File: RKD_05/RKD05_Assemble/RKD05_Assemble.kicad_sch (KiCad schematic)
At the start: 150 parts, among them J3 Conn_01x24, M1 Mark, M2 Mark, M3 Mark, M4 Mark, M5 Mark, M6 Mark, M7 Mark, SW1 SW_Push, SW10 SW_Push, SW11 SW_Push, SW12 SW_Push, SW13 SW_Push, SW14 SW_Push, SW15 SW_Push, SW16 SW_Push, SW17 SW_Push, SW18 SW_Push, SW19 SW_Push, SW2 SW_Push, SW20 SW_Push, SW21 SW_Push, SW22 SW_Push, SW23 SW_Push, SW24 SW_Push, SW25 SW_Push, SW26 SW_Push, SW27 SW_Push, SW28 SW_Push, SW29 SW_Push, SW3 SW_Push, SW30 SW_Push, SW4 SW_Push, SW40 RotaryEncoder_Switch, SW5 SW_Push, SW51 SW_Push, SW52 SW_Push, SW53 SW_Push, SW54 SW_Push, SW55 SW_Push, SW56 SW_Push, SW57 SW_Push, SW58 SW_Push, SW59 SW_Push, SW6 SW_Push, SW60 SW_Push, SW61 SW_Push, SW62 SW_Push, SW63 SW_Push, SW64 SW_Push, SW65 SW_Push, SW66 SW_Push, SW67 SW_Push, SW68 SW_Push, SW69 SW_Push, SW7 SW_Push, SW70 SW_Push, SW71 SW_Push, SW72 SW_Push, SW73 SW_Push, SW74 SW_Push, SW75 SW_Push, SW76 SW_Push, SW77 SW_Push, SW78 SW_Push, SW79 SW_Push, SW8 SW_Push, SW80 SW_Push, SW81 SW_Push, SW82 SW_Push, SW83 SW_Push, SW84 SW_Push, SW85 SW_Push, SW86 SW_Push, SW87 SW_Push, SW88 SW_Push, SW89 SW_Push, SW9 SW_Push, SW90 SW_Push

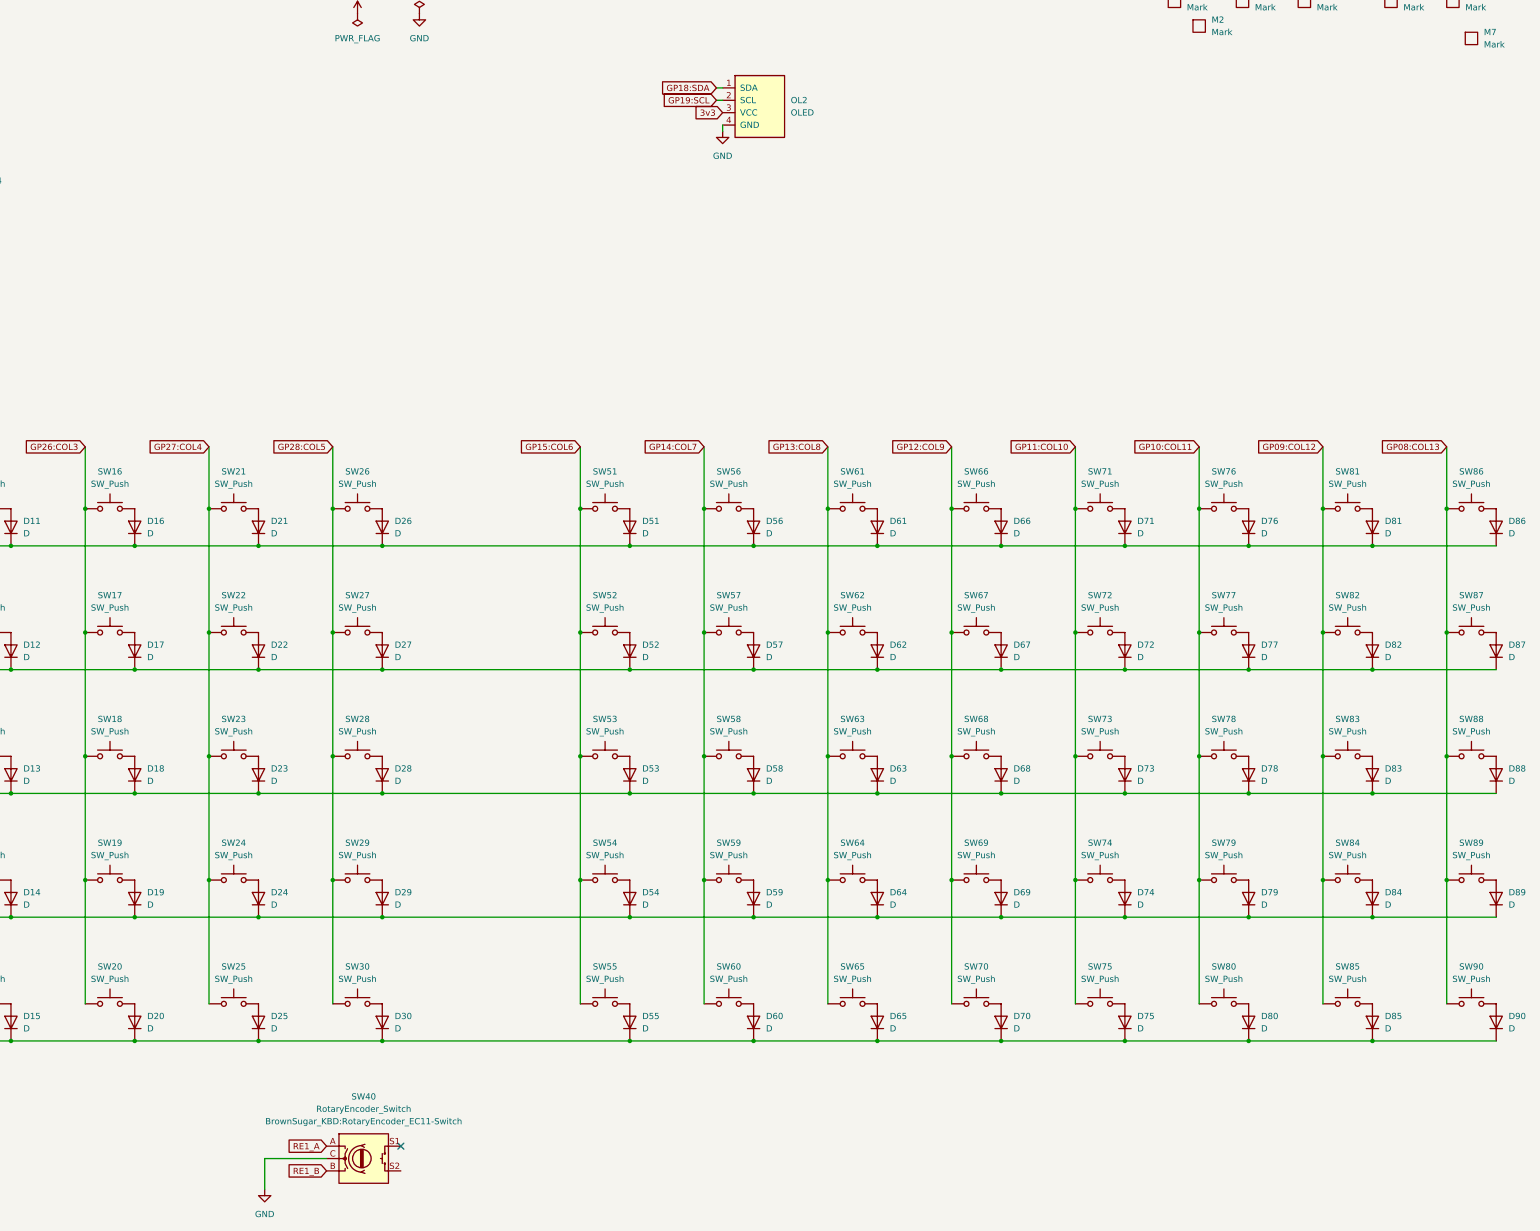
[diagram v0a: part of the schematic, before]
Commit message: RKD05　RE用PIN追加
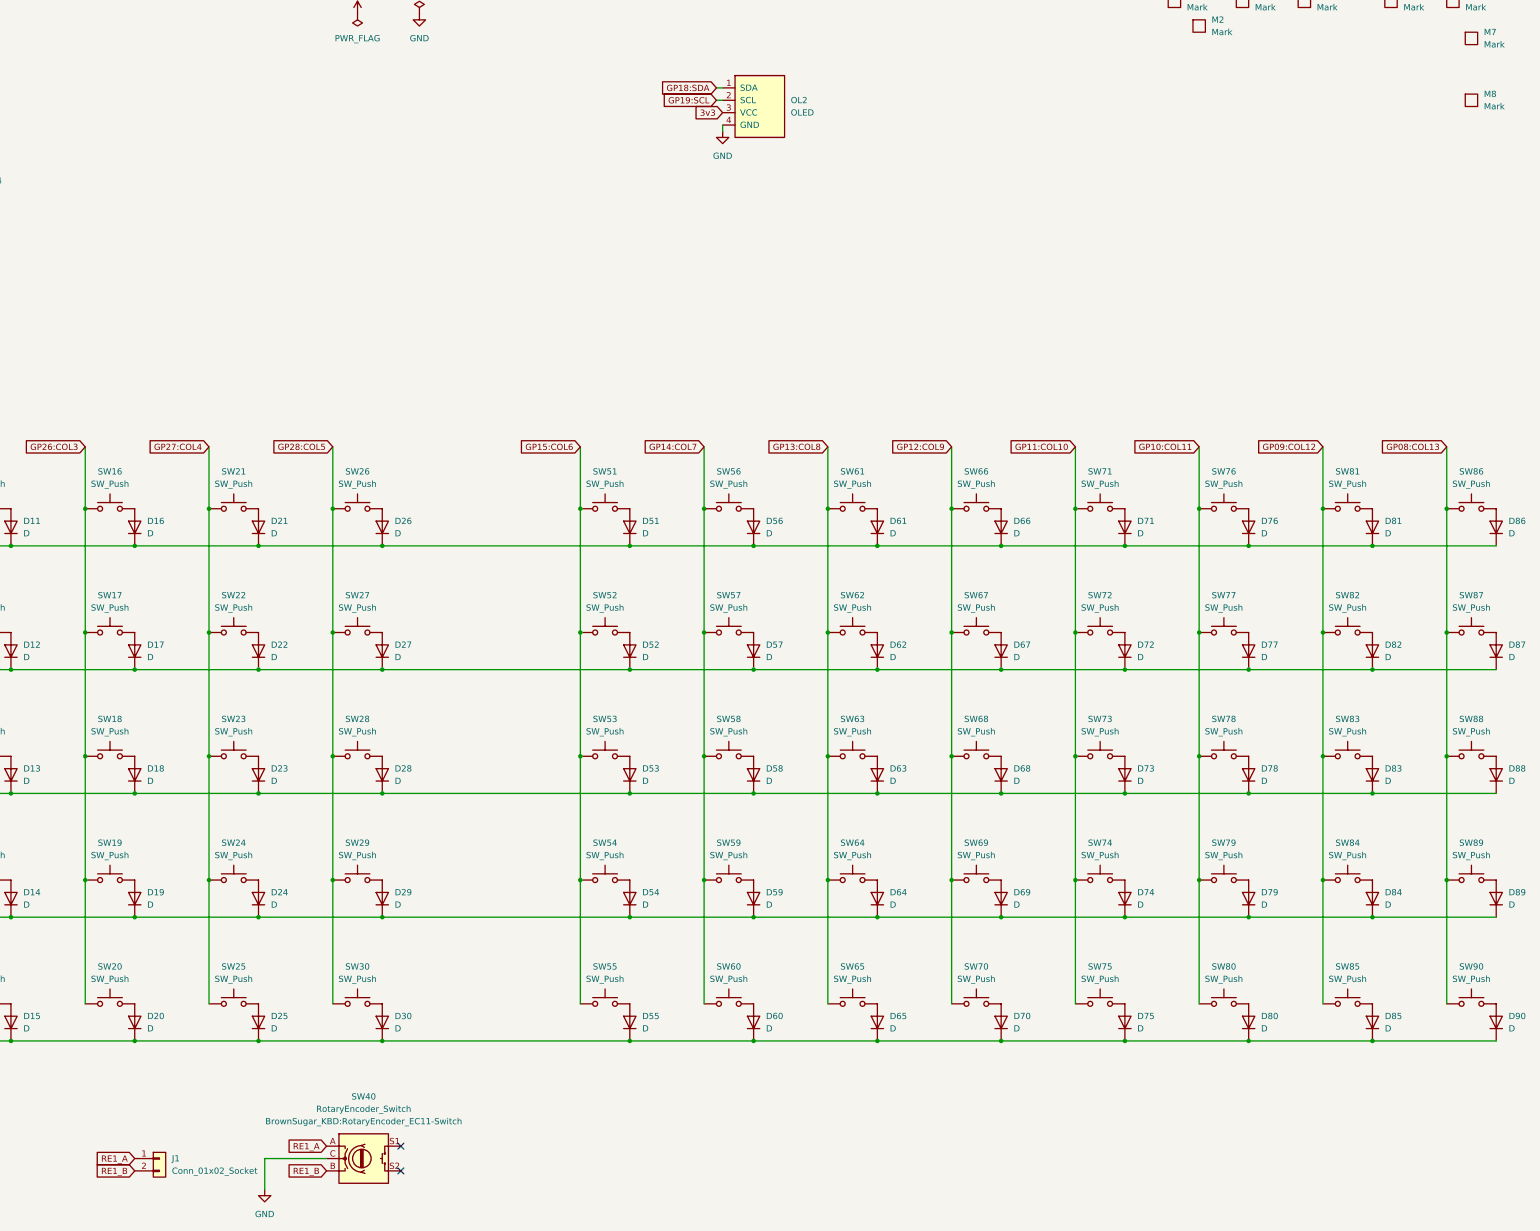
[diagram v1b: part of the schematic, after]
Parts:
- added J1: Conn_01x02_Socket, Connector_PinHeader_2.54mm:PinHeader_1x02_P2.54mm_Horizontal, symbol Connector_Generic:Conn_01x02
- added M8: Mark, Rikkodo_FootPrint:rkd_LOGO_2x, symbol BrownSugar_KBD:Mark
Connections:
- net RE1_A: now also J1.1 (Pin_1)
- net RE1_B: now also J1.2 (Pin_2)
- no-connect marks 1 -> 2
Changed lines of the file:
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@@
 	)
 	(no_connect
+		(at 173.99 262.89)
+	)
+	(no_connect
 		(at 173.99 257.81)
 	)
@@
 		)
 	)
+	(global_label "RE1_B"
+		(shape input)
+		(at 119.38 262.89 180)
+		(fields_autoplaced yes)
+		(effects
+			(font
+				(size 1.27 1.27)
+			)
+			(justify right)
+		)
+		(property "Intersheetrefs" "${INTERSHEET_REFS}"
+			(at 110.5287 262.89 0)
+			(effects
+				(font
+					(size 1.27 1.27)
+				)
+				(justify right)
+				(hide yes)
+			)
+		)
+	)
 	(global_label "GP15:COL6"
 		(shape input)
@@
 		)
 	)
+	(global_label "RE1_A"
+		(shape input)
+		(at 119.38 260.35 180)
+		(fields_autoplaced yes)
+		(effects
+			(font
+				(size 1.27 1.27)
+			)
+			(justify right)
+		)
+		(property "Intersheetrefs" "${INTERSHEET_REFS}"
+			(at 110.7101 260.35 0)
+			(effects
+				(font
+					(size 1.27 1.27)
+				)
+				(justify right)
+				(hide yes)
+			)
+		)
+	)
 	(global_label "GP20:ROW2"
 		(shape input)
@@
 	)
 	(symbol
+		(lib_id "BrownSugar_KBD:Mark")
+		(at 393.7 43.18 0)
+		(unit 1)
+		(exclude_from_sim no)
+		(in_bom yes)
+		(on_board yes)
+		(dnp no)
+		(fields_autoplaced yes)
+		(property "Reference" "M8"
+			(at 396.24 41.9099 0)
+			(effects
+				(font
+					(size 1.27 1.27)
+				)
+				(justify left)
+			)
+		)
+		(property "Value" "Mark"
+			(at 396.24 44.4499 0)
+			(effects
+				(font
+					(size 1.27 1.27)
+				)
+				(justify left)
+			)
+		)
+		(property "Footprint" "Rikkodo_FootPrint:rkd_LOGO_2x"
+			(at 393.7 43.18 0)
+			(effects
+				(font
+					(size 1.27 1.27)
+				)
+				(hide yes)
+			)
+		)
+		(property "Datasheet" ""
+			(at 393.7 43.18 0)
+			(effects
+				(font
+					(size 1.27 1.27)
+				)
+				(hide yes)
+			)
+		)
+		(property "Description" ""
+			(at 393.7 43.18 0)
+			(effects
+				(font
+					(size 1.27 1.27)
+				)
+				(hide yes)
+			)
+		)
+		(instances
+			(project "RKD05_Assemble"
+				(path "/01a859e0-5a12-4534-b9e3-6128f69eb8fc"
+					(reference "M8")
+					(unit 1)
+				)
+			)
+		)
+	)
+	(symbol
 		(lib_id "Switch:SW_Push")
 		(at 165.1 228.6 0)
@@
 					(unit 1)
 				)
+			)
+		)
+	)
+	(symbol
+		(lib_id "Connector_Generic:Conn_01x02")
+		(at 124.46 260.35 0)
+		(unit 1)
+		(exclude_from_sim no)
+		(in_bom yes)
+		(on_board yes)
+		(dnp no)
+		(fields_autoplaced yes)
+		(property "Reference" "J1"
+			(at 127 260.3499 0)
+			(effects
+				(font
+					(size 1.27 1.27)
+				)
+				(justify left)
+			)
+		)
+		(property "Value" "Conn_01x02_Socket"
+			(at 127 262.8899 0)
+			(effects
+				(font
+					(size 1.27 1.27)
+				)
+				(justify left)
+			)
+		)
+		(property "Footprint" "Connector_PinHeader_2.54mm:PinHeader_1x02_P2.54mm_Horizontal"
+			(at 124.46 260.35 0)
+			(effects
+				(font
+					(size 1.27 1.27)
+				)
+				(hide yes)
+			)
+		)
+		(property "Datasheet" "~"
+			(at 124.46 260.35 0)
+			(effects
+				(font
+					(size 1.27 1.27)
+				)
+				(hide yes)
+			)
+		)
+		(property "Description" "Generic connector, single row, 01x02, script generated (kicad-library-utils/schlib/autogen/connector/)"
+			(at 124.46 260.35 0)
+			(effects
+				(font
+					(size 1.27 1.27)
+				)
+				(hide yes)
+			)
+		)
+		(pin "1"
+		)
+		(pin "2"
+		)
+		(instances
+			(project ""
+				(path "/01a859e0-5a12-4534-b9e3-6128f69eb8fc"
+					(reference "J1")
+					(unit 1)
+				)

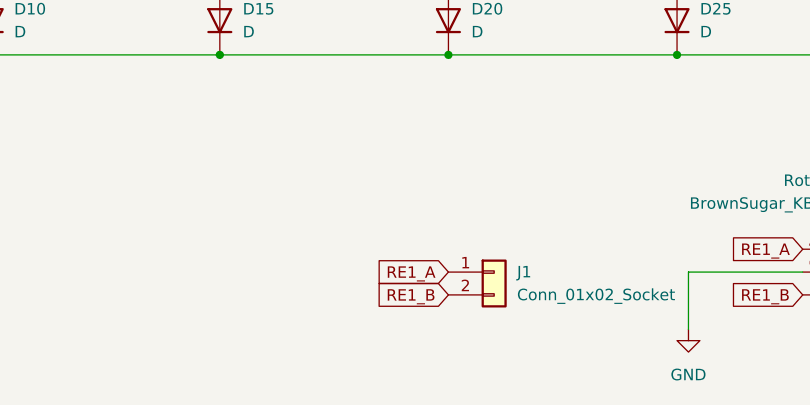
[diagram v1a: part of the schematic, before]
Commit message: RKD05 PinAssign変更’
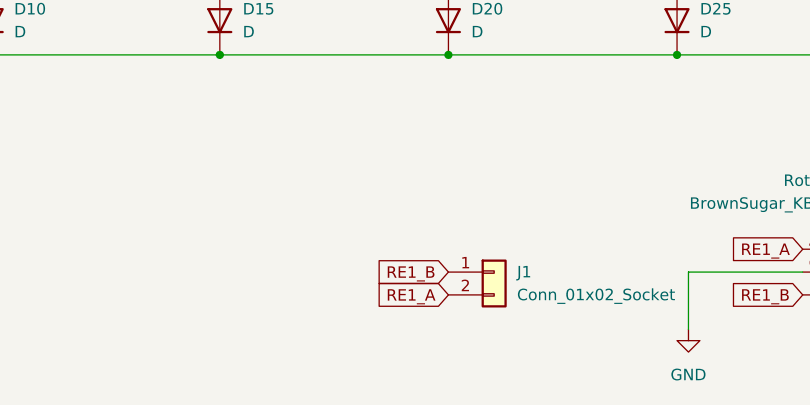
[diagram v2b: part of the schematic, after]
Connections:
- net RE1_A: now also J1.2 (Pin_2); no longer J1.1 (Pin_1)
- net RE1_B: now also J1.1 (Pin_1); no longer J1.2 (Pin_2)

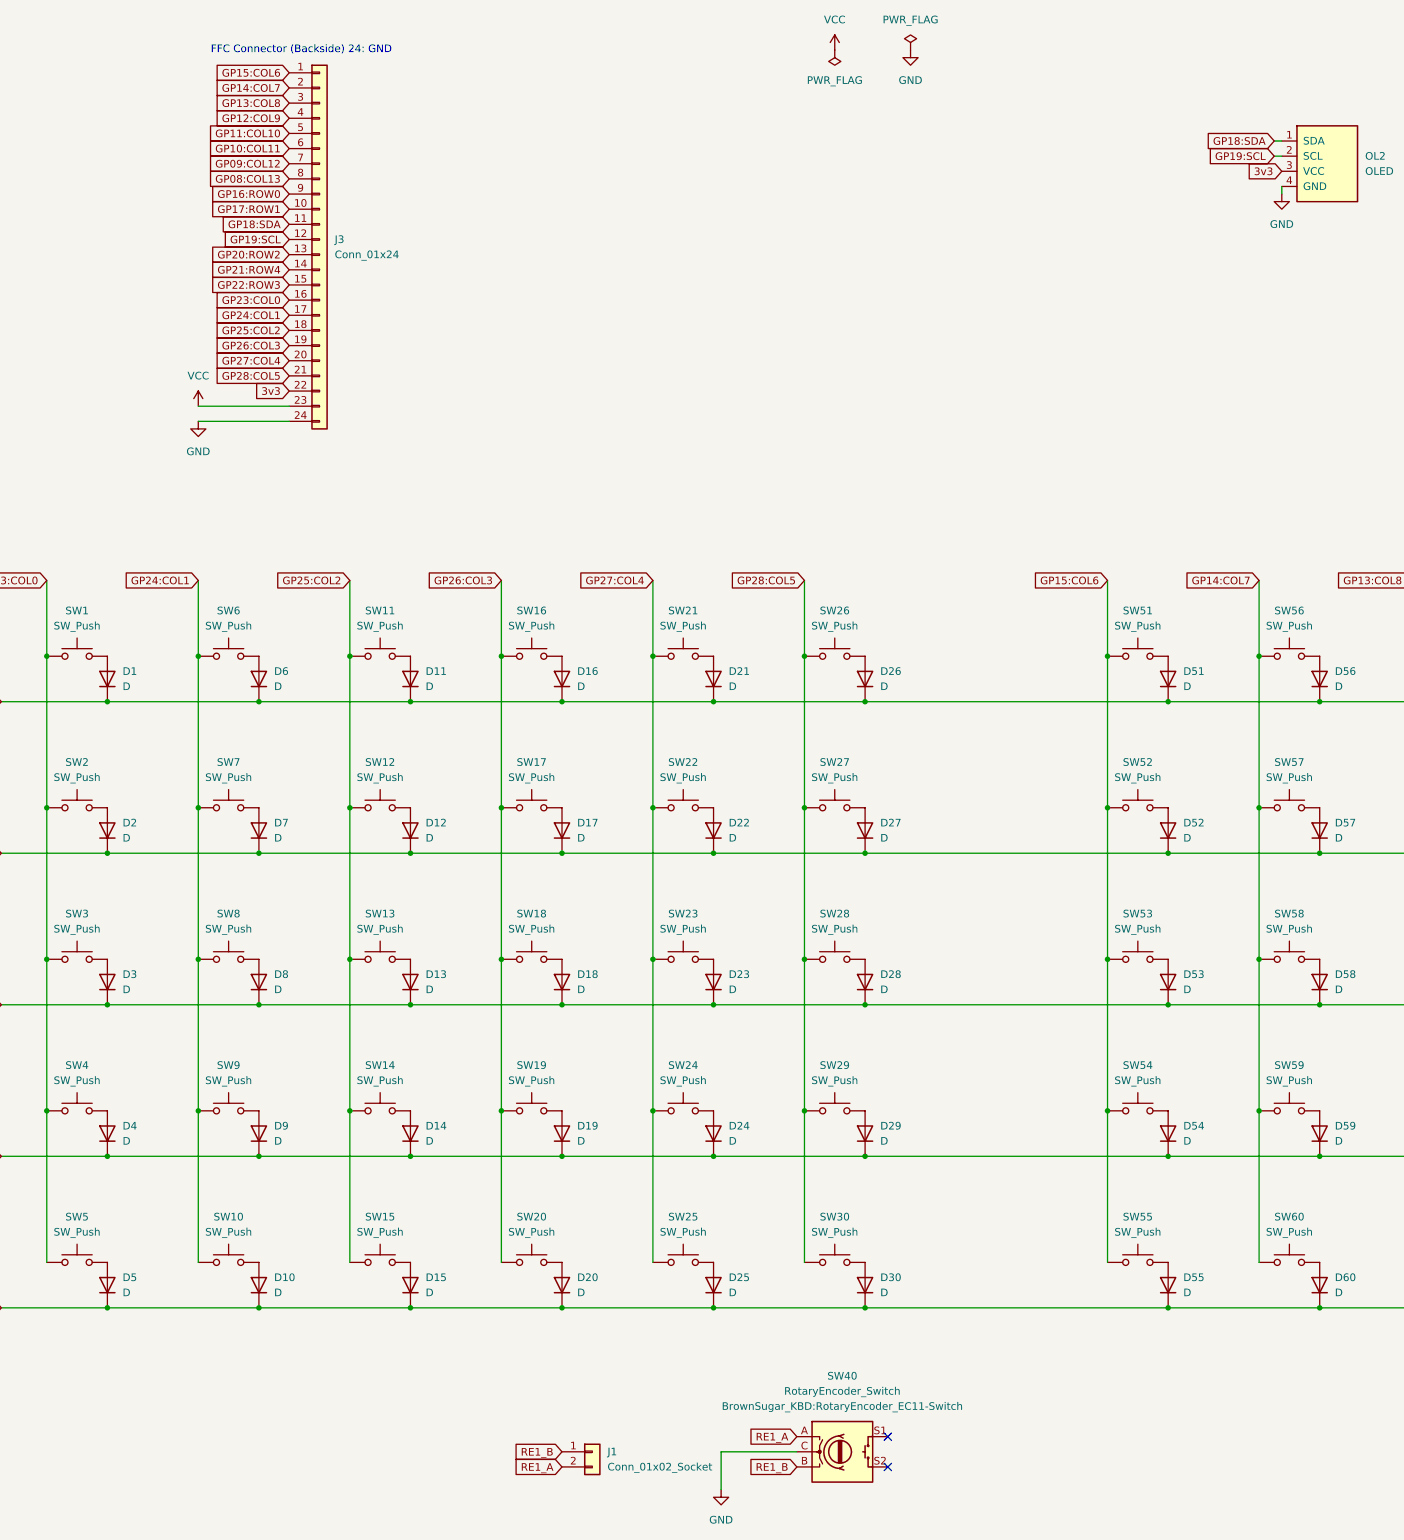
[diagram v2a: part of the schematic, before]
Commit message: RKD05接続名変更
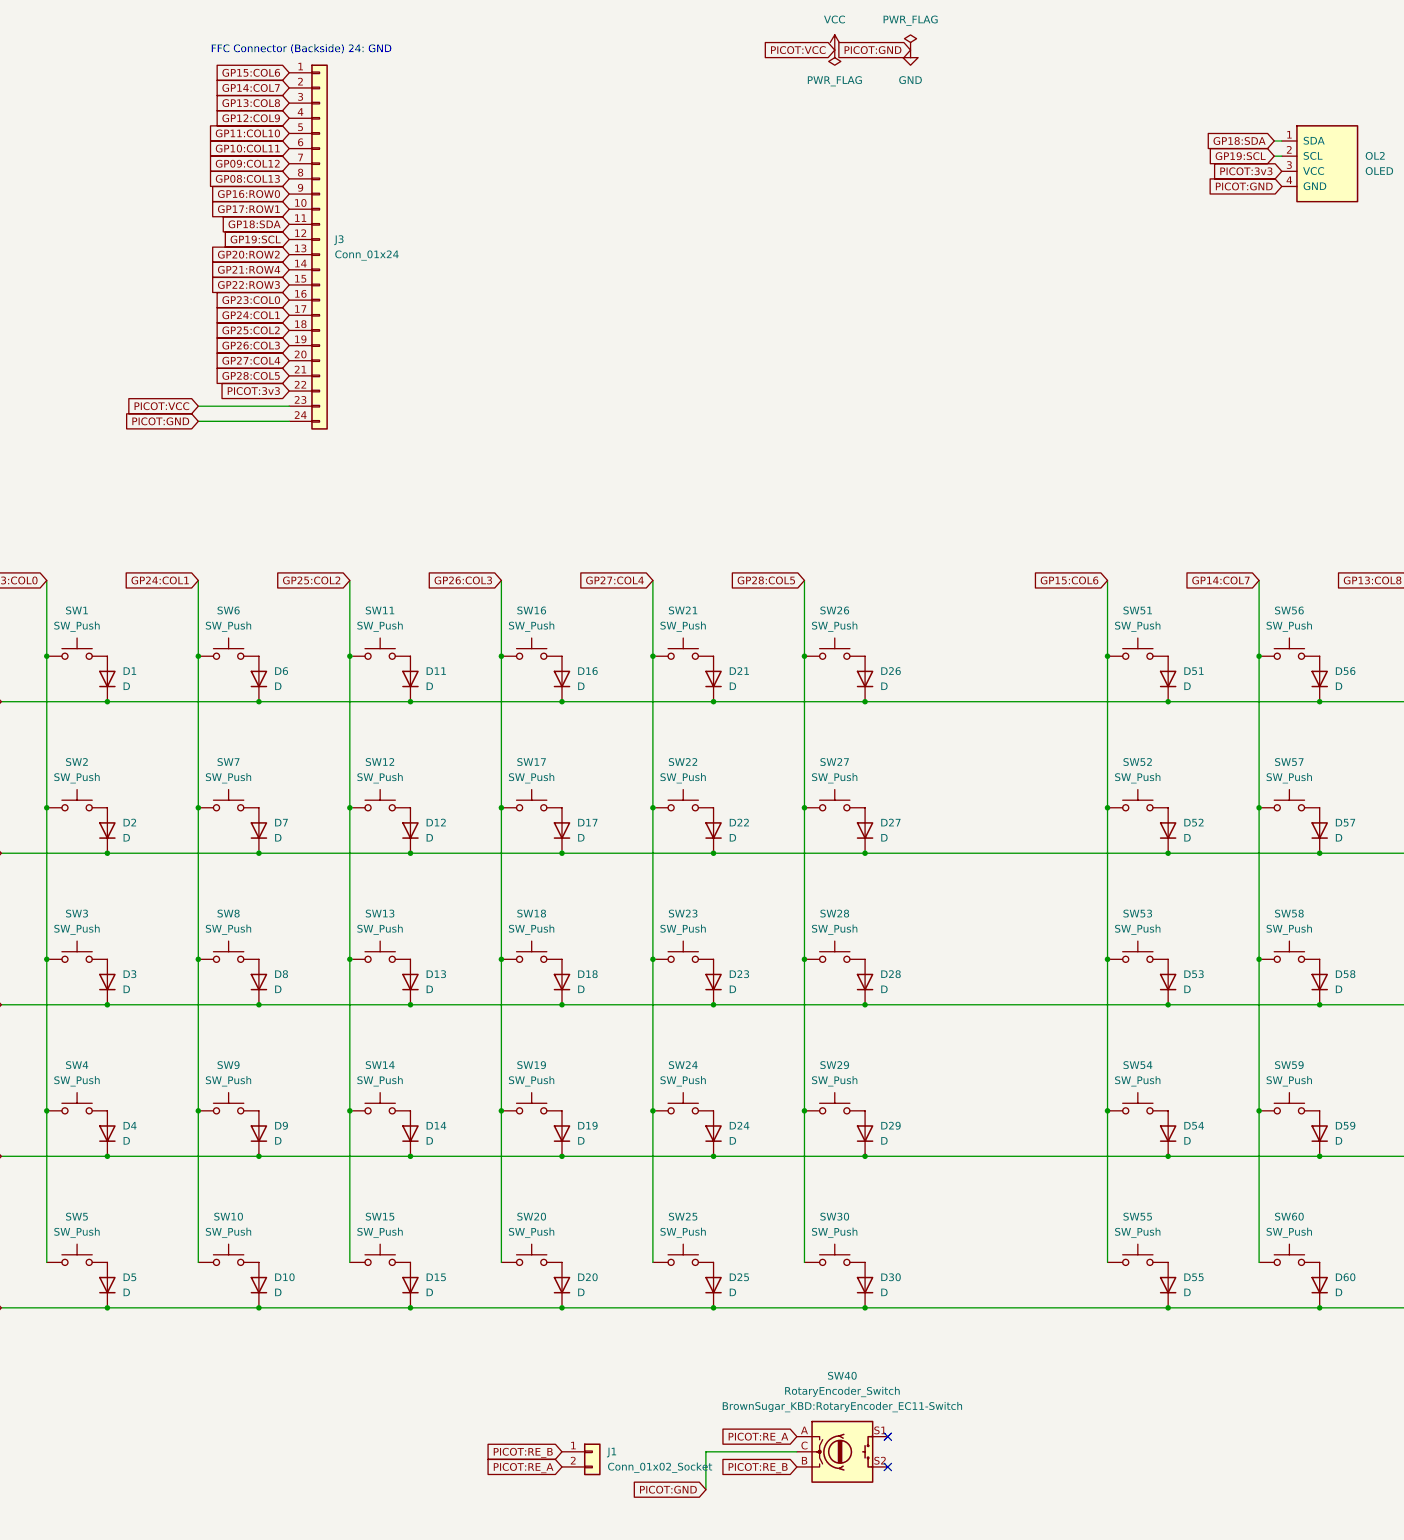
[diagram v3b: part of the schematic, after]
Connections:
- net 3v3 renamed PICOT:3v3
- net RE1_A renamed PICOT:RE_A
- net RE1_B renamed PICOT:RE_B
